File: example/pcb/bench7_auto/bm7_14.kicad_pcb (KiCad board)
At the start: 2 copper layers, 20.5 x 13.9 mm, 8 parts

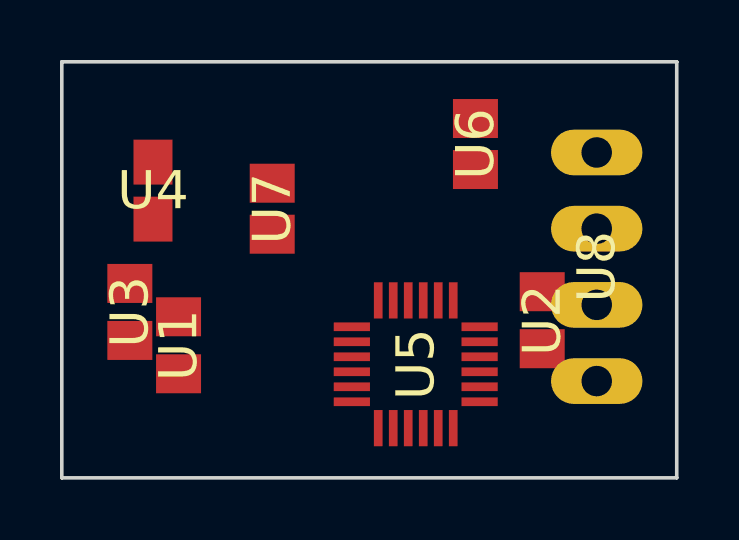
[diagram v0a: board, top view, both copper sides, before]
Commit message: refactor code of router
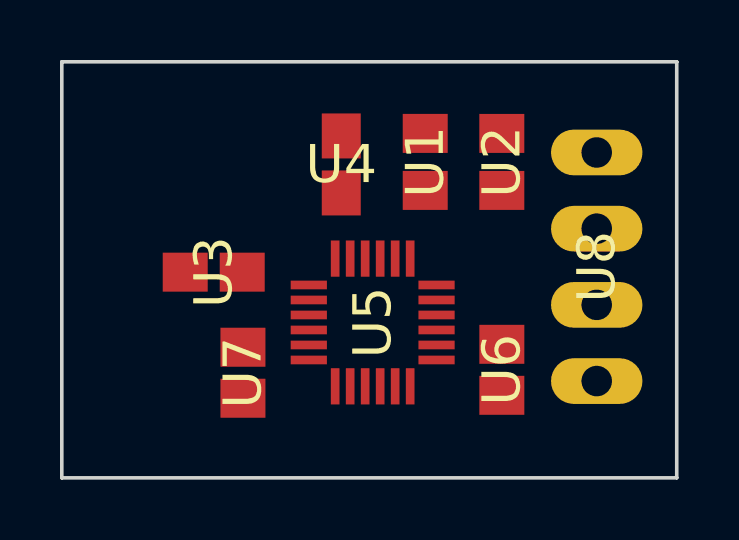
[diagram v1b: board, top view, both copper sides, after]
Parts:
- moved U1 10.2 mm to (150.4, 101.4), turned to 90 degrees
- moved U6 7.58 mm to (152.9, 108.3), turned to 90 degrees
- moved U4 6.34 mm to (147.6, 101.5)
- moved U7 5.55 mm to (144.3, 108.4), turned to 90 degrees
- moved U2 5.45 mm to (152.9, 101.4), turned to 90 degrees
- moved U3 3.09 mm to (143.3, 105.1), turned to 0 degrees
- moved U5 2.00 mm to (148.6, 106.8)
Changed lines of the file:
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@@
   (net 15 "Net-(U1-Pad1)")
   (footprint "imu:LGA-24" (layer "F.Cu")
-    (at 150.04996021696948 108.15149580317981 270.0)
+    (at 148.614606 106.758438 -90)
     (descr "<h3>LGA 4x4x1 mm 24-lead</h3>\n<ul><li>0.5mm pitch</li>\n<li>Pads are 0.35x0.2 mm square</li>\n</ul>\n<p>This package is used for:<p>\n<ul><li>ST Micro LSM9DS0 3D accel/gyro/mag</li></ul>")
     (attr through_hole)
@@
   )
   (footprint "imu:C0805" (layer "F.Cu")
-    (at 142.1438725130424 107.51864947643166 270.0)
+    (at 150.36627 101.406218 90)
     (descr "<b>CAPACITOR</b><p>")
     (attr through_hole)
@@
   )
   (footprint "imu:C0805" (layer "F.Cu")
-    (at 154.2660326466824 106.68293463932665 270.0)
+    (at 152.919068 101.406992 90)
     (descr "<b>CAPACITOR</b><p>")
     (attr through_hole)
@@
   )
   (footprint "imu:C0805" (layer "F.Cu")
-    (at 140.52097151892096 106.40648627742404 90.0)
+    (at 143.316325 105.081516)
     (descr "<b>CAPACITOR</b><p>")
     (attr through_hole)
@@
   )
   (footprint "imu:C0805" (layer "F.Cu")
-    (at 141.29168527653943 102.36210234971375 270.0)
+    (at 147.567288 101.490676 -90)
     (descr "<b>CAPACITOR</b><p>")
     (attr through_hole)
@@
   )
   (footprint "imu:R0805" (layer "F.Cu")
-    (at 152.04078901314722 100.810228052653 270.0)
+    (at 152.919984 108.33625 90)
     (descr "<b>RESISTOR</b><p>\nchip")
     (attr through_hole)
@@
   )
   (footprint "imu:R0805" (layer "F.Cu")
-    (at 145.26568211335643 102.96637692575004 270.0)
+    (at 144.290464 108.434115 90)
     (descr "<b>RESISTOR</b><p>\nchip")
     (attr through_hole)
